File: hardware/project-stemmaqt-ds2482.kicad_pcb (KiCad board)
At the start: 2 copper layers, 25.4 x 17.8 mm, 26 parts, among them J1 SM04B-SRSS-TB(LF)(SN), J2 SM04B-SRSS-TB(LF)(SN), J3 Conn_01x03_Male, J4 Conn_01x03_Male, Q1 Q_PMOS_GSD, U1 DS2482S-100+

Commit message: First placement done
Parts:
- removed J4: Conn_01x03_Male, Connector_PinHeader_2.54mm:PinHeader_1x03_P2.54mm_Vertical
- removed U$22: , stemmaqt_shift:ADAFRUIT_3.5MM
- removed U$25: , stemmaqt_shift:PCBFEAT-REV-040
- moved R1 32.4 mm to (52.5, 61.1), turned to 270 degrees
- moved R2 32.1 mm to (54.1, 61.1), turned to 270 degrees
- moved R3 26.6 mm to (54.0, 69.5), turned to 90 degrees
- moved JP1 25.3 mm to (51.7, 56.3)
- moved JP2 25.0 mm to (55.0, 56.3)
- moved R6 24.6 mm to (42.9, 56.0)
- moved D1 24.4 mm to (55.8, 69.5), turned to 90 degrees
- moved Q1 22.6 mm to (42.8, 58.5), turned to 180 degrees
- moved R5 22.2 mm to (52.5, 65.8), turned to 90 degrees
- moved JP3 20.9 mm to (46.7, 56.3)
- moved R4 19.3 mm to (54.1, 65.8), turned to 90 degrees
- moved J3 12.7 mm to (46.4, 70.0)
- moved U$31 3.52 mm to (39.1, 59.2)
- moved U$30 3.52 mm to (58.7, 68.1)
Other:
- board text added: "Stemma OneWire"
- board text removed: "A"
- board text removed: "Debug Stemma w/BitMagic"
- board text removed: "Stemma BitMagic"

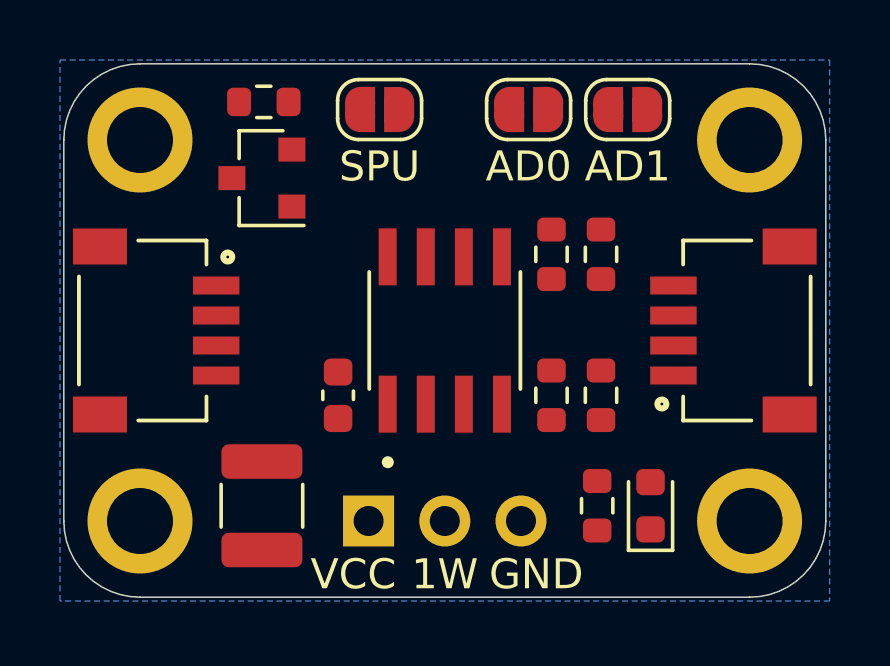
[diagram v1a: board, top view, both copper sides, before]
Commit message: Switch to 4 layers
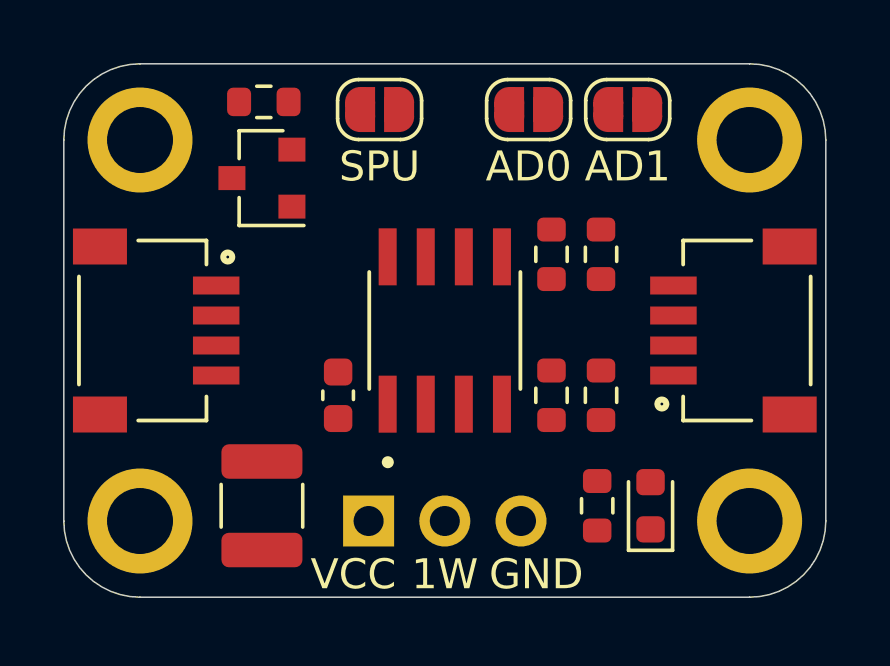
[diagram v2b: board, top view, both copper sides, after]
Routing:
- added copper zone on In1.Cu, net GND
- added copper zone on In2.Cu, net VCC
- removed copper zone on B.Cu, net GND
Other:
- copper layers 2 -> 4
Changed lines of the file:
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@@
   (layers
     (0 F.Cu signal)
+    (1 In1.Cu signal hide)
+    (2 In2.Cu signal hide)
     (31 B.Cu signal)
     (32 B.Adhes user hide)
     (33 F.Adhes user hide)
-    (34 B.Paste user hide)
-    (35 F.Paste user hide)
+    (34 B.Paste user)
+    (35 F.Paste user)
     (36 B.SilkS user)
     (37 F.SilkS user)
@@
     (40 Dwgs.User user hide)
     (41 Cmts.User user hide)
-    (42 Eco1.User user hide)
-    (43 Eco2.User user hide)
     (44 Edge.Cuts user)
     (45 Margin user hide)
@@
   (gr_line (start 38.735 72.517) (end 59.055 72.517) (layer Edge.Cuts) (width 0.05))
   (gr_arc (start 38.735 57.277) (end 38.735 54.737) (angle -90) (layer Edge.Cuts) (width 0.05))
-  (zone (net 1) (net_name GND) (layer B.Cu) (hatch edge 0.508)
+  (zone (net 1) (net_name GND) (layer In1.Cu) (hatch edge 0.508)
     (priority 6)
     (connect_pads (clearance 0.000001))
@@
     (polygon
       (pts
+        (xy 61.722 72.644) (xy 36.068 72.644) (xy 36.068 54.61) (xy 61.722 54.61)
+      )
+    )
+  )
+  (zone (net 2) (net_name VCC) (layer In2.Cu) (hatch edge 0.508)
+    (priority 6)
+    (connect_pads (clearance 0.000001))
+    (min_thickness 0.127)
+    (fill yes (arc_segments 32) (thermal_gap 0.304) (thermal_bridge_width 0.304))
+    (polygon
+      (pts

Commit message: Routing done
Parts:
- moved R1 1.65 mm to (54.1, 61.1)
- moved R2 1.65 mm to (52.5, 61.1)
- moved R4 1.65 mm to (52.5, 65.8)
- moved R5 1.65 mm to (54.1, 65.8)
- turned C1 to 270 degrees
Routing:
- net /1WIRE: track 0.00 -> 32.3 mm
- net /SDA: track 0.00 -> 24.9 mm
- net /SCL: track 0.00 -> 19.1 mm
- net GND: track 0.00 -> 15.9 mm, vias 0 -> 11
- net VCC: track 0.00 -> 14.9 mm, vias 0 -> 9
- net Net-(JP2-Pad2): track 0.00 -> 13.5 mm, vias 0 -> 2
- net Net-(JP1-Pad2): track 0.00 -> 12.3 mm
- net /PCTLZ: track 0.00 -> 7.27 mm, vias 0 -> 2
- net Net-(JP3-Pad1): track 0.00 -> 5.66 mm
- net Net-(D1-Pad2): track 0.00 -> 1.79 mm
- net Net-(Q1-Pad2): track 0.00 -> 1.64 mm

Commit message: Add version of previous commit
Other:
- board text added: "v1.0.0"
